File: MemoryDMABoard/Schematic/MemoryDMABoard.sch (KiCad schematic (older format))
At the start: 32 parts, among them U19 MCM6665, U20 MCM6665, U21 MCM6665, U22 MCM6665, U23 MCM6665, U24 MCM6665, U25 MCM6665, U26 MCM6665, U27 MCM6665, U28 MCM6665, U29 MCM6665, U30 MCM6665, U31 MCM6665, U32 MCM6665, U33 MCM6665, U34 MCM6665, U35 MCM6665, U36 MCM6665, U37 MCM6665, U38 MCM6665, U39 MCM6665, U40 MCM6665, U41 MCM6665, U42 MCM6665, U43 MCM6665, U44 MCM6665, U45 MCM6665, U46 MCM6665, U47 MCM6665, U48 MCM6665, U49 MCM6665, U50 MCM6665

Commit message: Add ISA bus and labels to MemoryDMABoard.
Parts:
- added C19, C20, C21, C22, C23, C24, C25, C26, C27, C28, C29, C30, C31, C32, C33, C34, C35, C36, C37, C38, C39, C40, C41, C42, C43, C44, C45, C46, C47, C48, C49, C50, C51, C52, C53, C54, C55, C56: 0.1uF, symbol Device:C
- added J0: Bus_ISA_8bit, symbol 00Custom:Bus_ISA_8bit
- added R10, R8: 56R, symbol Device:R
- added R5, R6, R7, R9: 33R, symbol Device:R
- added RP1: 56R, symbol Device:R_Pack08
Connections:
- net +5V: now also C19.1, C20.1, C21.1, C22.1, C23.1, C24.1, C25.1, C26.1, C27.1, C28.1, C29.1, C30.1, C31.1, C32.1, C33.1, C34.1, C35.1, C36.1, C37.1, C38.1, C39.1, C40.1, C41.1, C42.1, C43.1, C44.1, C45.1, C46.1, C47.1, C48.1, C49.1, C50.1, C51.1, C52.1, C53.1, C54.1, C55.1, C56.1, J0.3 (VCC)
- net DMA00: now also RP1.3 (R3.1)
- net DMA01: now also RP1.6 (R6.1)
- net DMA02: now also RP1.2 (R2.1)
- net DMA03: now also RP1.1 (R1.1)
- net DMA04: now also RP1.8 (R8.1)
- net DMA05: now also RP1.5 (R5.1)
- net DMA06: now also RP1.4 (R4.1)
- net DMA07: now also RP1.7 (R7.1)
- net GND: now also C19.2, C20.2, C21.2, C22.2, C23.2, C24.2, C25.2, C26.2, C27.2, C28.2, C29.2, C30.2, C31.2, C32.2, C33.2, C34.2, C35.2, C36.2, C37.2, C38.2, C39.2, C40.2, C41.2, C42.2, C43.2, C44.2, C45.2, C46.2, C47.2, C48.2, C49.2, C50.2, C51.2, C52.2, C53.2, C54.2, C55.2, C56.2, J0.1 (GND), J0.10 (GND), J0.31 (GND)
- net _~CAS: now also R8.1
- net _~RAS0: now also R5.1
- net _~RAS1: now also R6.1
- net _~RAS2: now also R7.1
- net _~RAS3: now also R9.1
- net _~WR: now also R10.1
- new net AEN: J0.42 (AEN)
- new net BUSA00: J0.62 (BA00)
- new net BUSA01: J0.61 (BA01)
- new net BUSA02: J0.60 (BA02)
- new net BUSA03: J0.59 (BA03)
- new net BUSA04: J0.58 (BA04)
- new net BUSA05: J0.57 (BA05)
- new net BUSA06: J0.56 (BA06)
- new net BUSA07: J0.55 (BA07)
- new net BUSA08: J0.54 (BA08)
- new net BUSA09: J0.53 (BA09)
- new net BUSA10: J0.52 (BA10)
- new net BUSA11: J0.51 (BA11)
- new net BUSA12: J0.50 (BA12)
- new net BUSA13: J0.49 (BA13)
- new net BUSA14: J0.48 (BA14)
- new net BUSA15: J0.47 (BA15)
- new net BUSA16: J0.46 (BA16)
- new net BUSA17: J0.45 (BA17)
- new net BUSA18: J0.44 (BA18)
- new net BUSA19: J0.43 (BA19)
- new net BUSD00: J0.40 (DB0)
- new net BUSD01: J0.39 (DB1)
- new net BUSD02: J0.38 (DB2)
- new net BUSD03: J0.37 (DB3)
- new net BUSD04: J0.36 (DB4)
- new net BUSD05: J0.35 (DB5)
- new net BUSD06: J0.34 (DB6)
- new net BUSD07: J0.33 (DB7)
- new net CLK: J0.20 (CLK)
- new net DMATC: J0.27 (TC)
- new net MA00: RP1.14 (R3.2)
- new net MA01: RP1.11 (R6.2)
- new net MA02: RP1.15 (R2.2)
- new net MA03: RP1.16 (R1.2)
- new net MA04: RP1.9 (R8.2)
- new net MA05: RP1.12 (R5.2)
- new net MA06: RP1.13 (R4.2)
- new net MA07: RP1.10 (R7.2)
- new net OSC: J0.30 (OSC)
- new net READY: J0.41 (IO_READY)
- new net RESET: J0.2 (RESET)
- new net ~BREQ: J0.22 (IRQ6)
- new net ~CAS: R8.2
- new net ~DACK1: J0.17 (~DACK1)
- new net ~DACK3: J0.15 (~DACK3)
- new net ~DRQ1: J0.18 (DRQ1)
- new net ~DRQ3: J0.16 (DRQ3)
- new net ~FDCDMACK: J0.26 (~DACK2)
- new net ~FDCDMARQ: J0.6 (DRQ2)
- new net ~IOR: J0.14 (~IOR)
- new net ~IOW: J0.13 (~IOW)
- new net ~MEMR: J0.12 (~SMEMR)
- new net ~MEMW: J0.11 (~SMEMW)
- new net ~RAS0: R5.2
- new net ~RAS1: R6.2
- new net ~RAS2: R7.2
- new net ~RAS3: R9.2
- new net ~REFRESH: J0.19 (~DACK0)
- new net ~RFSHRQ: J0.21 (IRQ7)
- new net ~WR: R10.2
- no-connect marks 32 -> 42
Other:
- note added: "DRAM SECTION (Tandy Schematic Sheet 2)"
- note added: "NOTE: Bus pin numbers are flipped \nfrom the Tandy Schematic. Tandy \nnumbers are 1-31 down the right \nside and 32-62 down the left side."
- moved on the sheet: U19, U20, U21, U22, U23, U24, U25, U26, U27, U28, U29, U30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

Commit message: Add ISA BUS buffering to MemoryDMABoard schematic.
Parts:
- added C1, C10, C11, C12, C13, C14, C15, C16, C17, C18, C2, C3, C4, C5, C6, C7, C8, C9: 0.1uF, symbol Device:C
- added R3: 2K2, symbol Device:R
- added U1, U11, U7: 74LS244, symbol 74xx:74LS244
- added U15, U17: 74LS245, symbol 74xx:74LS245
- added U2: 74LS04, symbol 74xx:74LS04
- added U?: 8237, Package_DIP:DIP-40_W15.24mm, symbol Interface:8237
- C51, C52, C53, C54, C55, C56: value 0.1uF -> 68uF; symbol Device:C -> Device:CP
- renumbered J0 to J1
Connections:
- net +5V: now also C1.1, C10.1, C11.1, C12.1, C13.1, C14.1, C15.1, C16.1, C17.1, C18.1, C2.1, C3.1, C4.1, C5.1, C6.1, C7.1, C8.1, C9.1, R3.1, U1.20 (VCC), U11.20 (VCC), U15.20 (VCC), U17.20 (VCC), U7.20 (VCC)
- net AEN: now also U1.4 (I1a)
- net BUSA00: now also U15.14 (B4)
- net BUSA01: now also U15.13 (B5)
- net BUSA02: now also U15.12 (B6)
- net BUSA03: now also U15.11 (B7)
- net BUSA04: now also U11.2 (I0a)
- net BUSA05: now also U11.15 (I2b)
- net BUSA06: now also U11.13 (I1b)
- net BUSA07: now also U11.4 (I1a)
- net BUSA08: now also U7.11 (I0b)
- net BUSA09: now also U7.13 (I1b)
- net BUSA10: now also U7.15 (I2b)
- net BUSA11: now also U7.17 (I3b)
- net BUSA12: now also U7.8 (I3a)
- net BUSA13: now also U7.6 (I2a)
- net BUSA14: now also U7.4 (I1a)
- net BUSA15: now also U7.2 (I0a)
- net BUSA16: now also U1.8 (I3a)
- net BUSA17: now also U1.11 (I0b)
- net BUSA18: now also U1.13 (I1b)
- net BUSA19: now also U1.17 (I3b)
- net BUSD00: now also U17.18 (B0)
- net BUSD01: now also U17.17 (B1)
- net BUSD02: now also U17.16 (B2)
- net BUSD03: now also U17.15 (B3)
- net BUSD04: now also U17.14 (B4)
- net BUSD05: now also U17.13 (B5)
- net BUSD06: now also U17.12 (B6)
- net BUSD07: now also U17.11 (B7)
- net CLK: now also U1.15 (I2b)
- net D00: now also U17.2 (A0)
- net D01: now also U17.3 (A1)
- net D02: now also U17.4 (A2)
- net D03: now also U17.5 (A3)
- net D04: now also U17.6 (A4)
- net D05: now also U17.7 (A5)
- net D06: now also U17.8 (A6)
- net D07: now also U17.9 (A7)
- net DMATC: now also U11.9 (O0b)
- net GND: now also C1.2, C10.2, C11.2, C12.2, C13.2, C14.2, C15.2, C16.2, C17.2, C18.2, C2.2, C3.2, C4.2, C5.2, C6.2, C7.2, C8.2, C9.2, U1.1 (OEa), U1.10 (GND), U1.19 (OEb), U11.1 (OEa), U11.10 (GND), U11.19 (OEb), U15.10 (GND), U15.19 (CE), U17.10 (GND), U7.1 (OEa), U7.10 (GND), U7.19 (OEb)
- net OSC: now also U11.8 (I3a)
- net READY: now also U1.6 (I2a)
- net RESET: now also U1.2 (I0a)
- net ~BREQ: now also U11.3 (O3b)
- net ~IOR: now also U15.15 (B3)
- net ~IOW: now also U15.16 (B2)
- net ~MEMR: now also U15.17 (B1)
- net ~MEMW: now also U15.18 (B0)
- new net A00: U15.6 (A4)
- new net A01: U15.7 (A5)
- new net A02: U15.8 (A6)
- new net A03: U15.9 (A7)
- new net A04: U11.18 (O0a)
- new net A05: U11.5 (O2b)
- new net A06: U11.7 (O1b)
- new net A07: U11.16 (O1a)
- new net A08: U7.9 (O0b)
- new net A09: U7.7 (O1b)
- new net A10: U7.5 (O2b)
- new net A11: U7.3 (O3b)
- new net A12: U7.12 (O3a)
- new net A13: U7.14 (O2a)
- new net A14: U7.16 (O1a)
- new net A15: U7.18 (O0a)
- new net A16: U1.12 (O3a)
- new net A17: U1.9 (O0b)
- new net A18: U1.7 (O1b)
- new net A19: U1.3 (O3b)
- new net BRDY: U1.14 (O2a)
- new net DBDIR: U17.1 (A->B)
- new net DMAAEN: U15.1 (A->B)
- new net DMACLK: U2.6, U?.12 (CLK)
- new net HSCLK: U11.12 (O3a)
- new net _8237_HLDA: U1.16 (O1a), U?.7 (HLDA)
- new net _8237_HRQ: U2.1, U?.10 (HRQ)
- new net _8237_RESET: U1.18 (O0a), U?.13 (RESET)
- new net _8237_~EOP: R3.2, U2.3, U?.36 (~EOP~)
- new net _CLK_BUF: U1.5 (O2b), U2.5
- new net _DMATC_UNBUF: U11.11 (I0b), U2.4
- new net _~BREQ~_UNBUF: U11.17 (I3b), U2.2
- new net ~DBEN: U17.19 (CE)
- new net ~IR: U15.5 (A3)
- new net ~IW: U15.4 (A2)
- new net ~MR: U15.3 (A1)
- new net ~MW: U15.2 (A0)
- no-connect marks 42 -> 44
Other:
- note added: "BUS Buffering"
- note added: "ISA BUS"
- moved on the sheet: C19, C20, C21, C22, C23, C24, C25, C26, C27, C28, C29, C30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

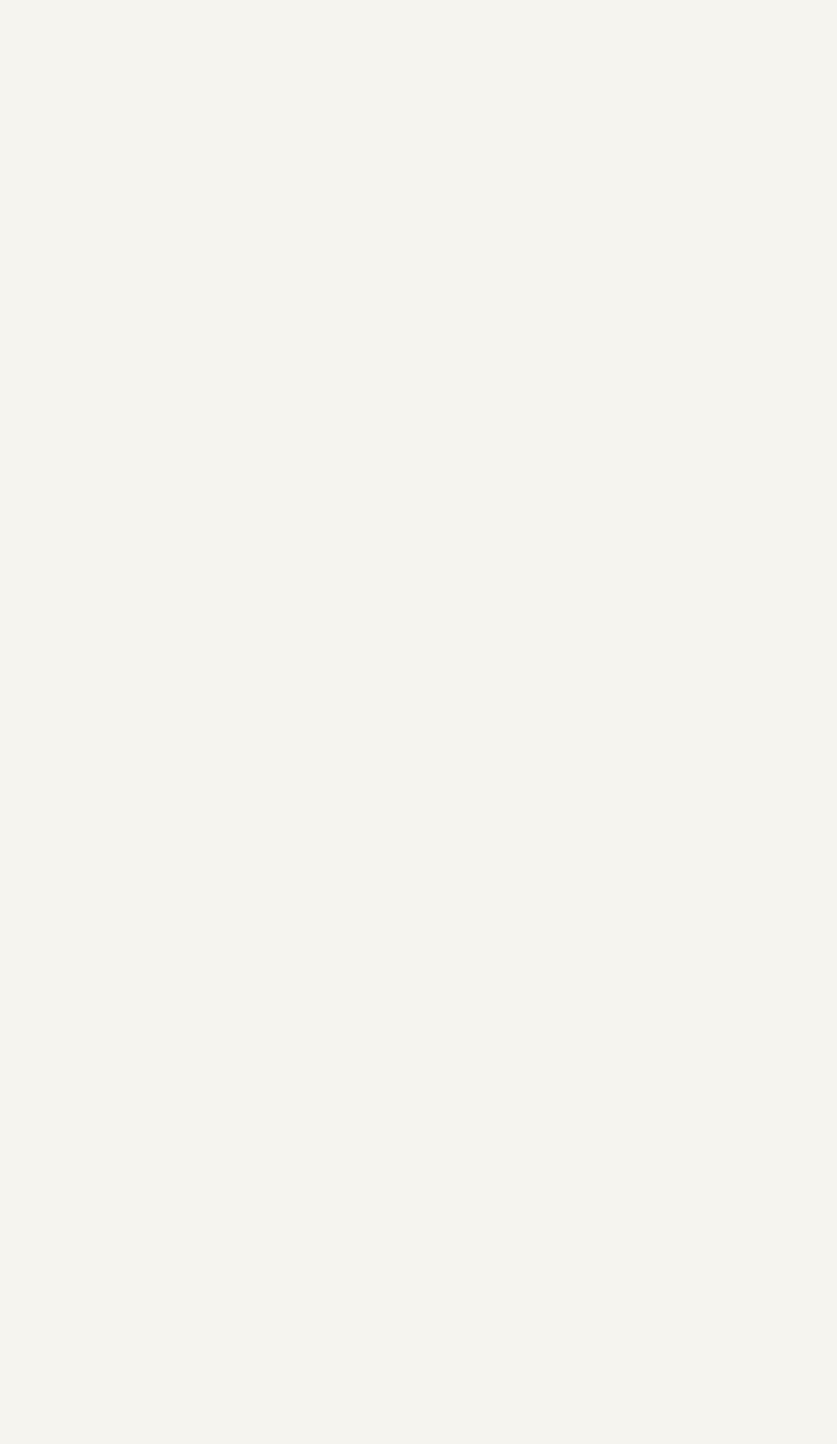
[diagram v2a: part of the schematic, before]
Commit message: Add DRAM address multiplexing.
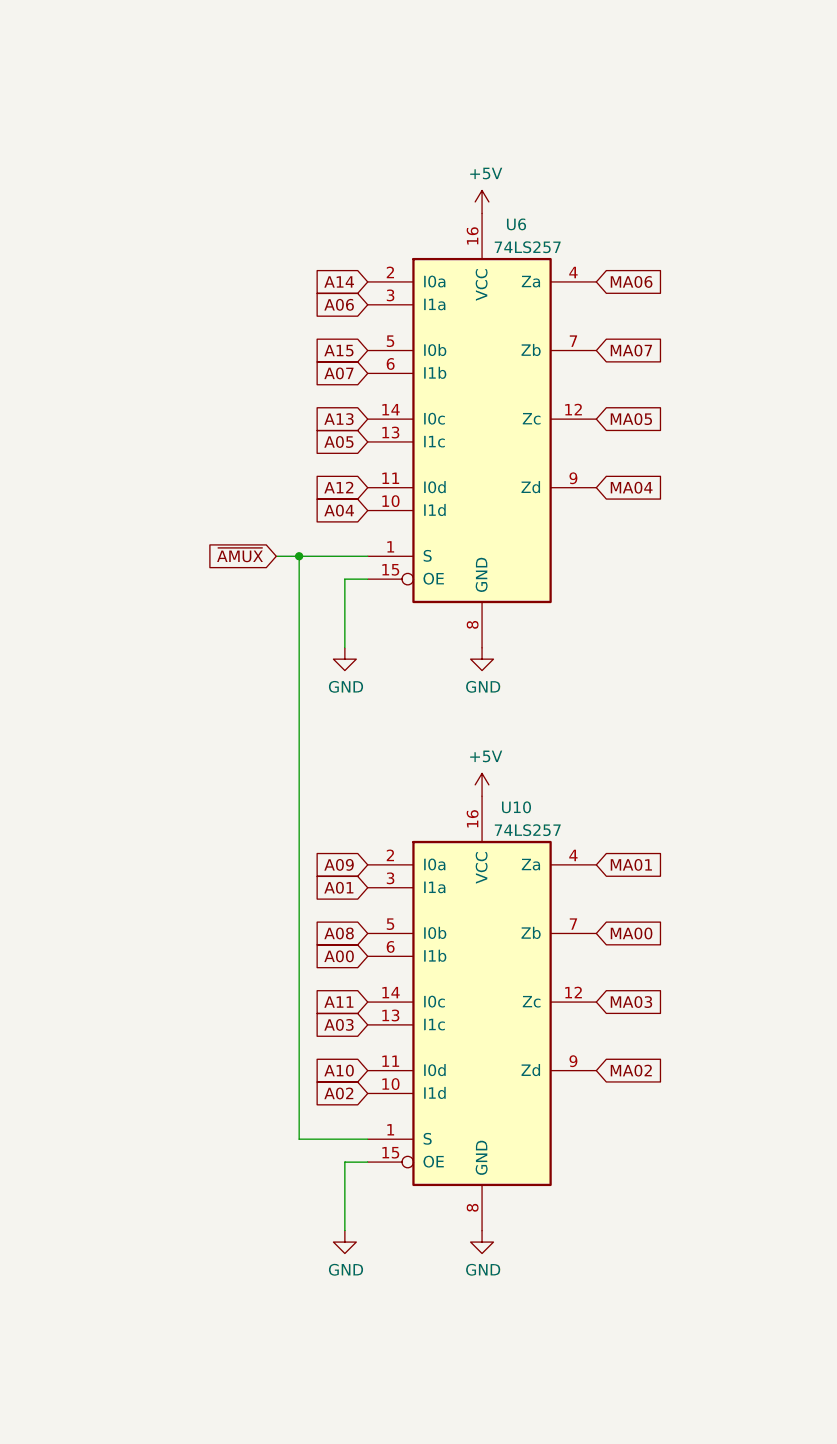
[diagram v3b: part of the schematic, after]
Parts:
- added U10, U6: 74LS257, symbol 74xx:74LS257
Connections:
- net +5V: now also U10.16 (VCC), U6.16 (VCC)
- net A00: now also U10.6 (I1b)
- net A01: now also U10.3 (I1a)
- net A02: now also U10.10 (I1d)
- net A03: now also U10.13 (I1c)
- net A04: now also U6.10 (I1d)
- net A05: now also U6.13 (I1c)
- net A06: now also U6.3 (I1a)
- net A07: now also U6.6 (I1b)
- net A08: now also U10.5 (I0b)
- net A09: now also U10.2 (I0a)
- net A10: now also U10.11 (I0d)
- net A11: now also U10.14 (I0c)
- net A12: now also U6.11 (I0d)
- net A13: now also U6.14 (I0c)
- net A14: now also U6.2 (I0a)
- net A15: now also U6.5 (I0b)
- net GND: now also U10.15 (OE), U10.8 (GND), U6.15 (OE), U6.8 (GND)
- net MA00: now also U10.7 (Zb)
- net MA01: now also U10.4 (Za)
- net MA02: now also U10.9 (Zd)
- net MA03: now also U10.12 (Zc)
- net MA04: now also U6.9 (Zd)
- net MA05: now also U6.12 (Zc)
- net MA06: now also U6.4 (Za)
- net MA07: now also U6.7 (Zb)
- new net ~AMUX: U10.1 (S), U6.1 (S)
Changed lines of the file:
@@
 Text Notes 1250 1000 0    118  ~ 0
 ISA BUS
+$Comp
+L 74xx:74LS257 U6
+U 1 1 606B6E2F
+P 27100 25200
+F 0 "U6" H 27250 26050 50  0000 C CNN
+F 1 "74LS257" H 27300 25950 50  0000 C CNN
+F 2 "" H 27100 25200 50  0001 C CNN
+F 3 "http://www.ti.com/lit/gpn/sn74LS257" H 27100 25200 50  0001 C CNN
+	1    27100 25200
+	1    0    0    -1
+$EndComp
+$Comp
+L power:GND #PWR?
+U 1 1 606B9008
+P 27100 26200
+F 0 "#PWR?" H 27100 25950 50  0001 C CNN
+F 1 "GND" H 27105 26027 50  0000 C CNN
+F 2 "" H 27100 26200 50  0001 C CNN
+F 3 "" H 27100 26200 50  0001 C CNN
+	1    27100 26200
+	1    0    0    -1
+$EndComp
+$Comp
+L power:+5V #PWR?
+U 1 1 606B972A
+P 27100 24300
+F 0 "#PWR?" H 27100 24150 50  0001 C CNN
+F 1 "+5V" H 27115 24473 50  0000 C CNN
+F 2 "" H 27100 24300 50  0001 C CNN
+F 3 "" H 27100 24300 50  0001 C CNN
+	1    27100 24300
+	1    0    0    -1
+$EndComp
+$Comp
+L power:GND #PWR?
+U 1 1 606BA42C
+P 26500 26200
+F 0 "#PWR?" H 26500 25950 50  0001 C CNN
+F 1 "GND" H 26505 26027 50  0000 C CNN
+F 2 "" H 26500 26200 50  0001 C CNN
+F 3 "" H 26500 26200 50  0001 C CNN
+	1    26500 26200
+	1    0    0    -1
+$EndComp
+Wire Wire Line
+	26600 25900 26500 25900
+Wire Wire Line
+	26500 25900 26500 26200
+$Comp
+L 74xx:74LS257 U10
+U 1 1 606D1323
+P 27100 27750
+F 0 "U10" H 27250 28600 50  0000 C CNN
+F 1 "74LS257" H 27300 28500 50  0000 C CNN
+F 2 "" H 27100 27750 50  0001 C CNN
+F 3 "http://www.ti.com/lit/gpn/sn74LS257" H 27100 27750 50  0001 C CNN
+	1    27100 27750
+	1    0    0    -1
+$EndComp
+$Comp
+L power:GND #PWR?
+U 1 1 606D2B39
+P 27100 28750
+F 0 "#PWR?" H 27100 28500 50  0001 C CNN
+F 1 "GND" H 27105 28577 50  0000 C CNN
+F 2 "" H 27100 28750 50  0001 C CNN
+F 3 "" H 27100 28750 50  0001 C CNN
+	1    27100 28750
+	1    0    0    -1
+$EndComp
+$Comp
+L power:+5V #PWR?
+U 1 1 606D2B43
+P 27100 26850
+F 0 "#PWR?" H 27100 26700 50  0001 C CNN
+F 1 "+5V" H 27115 27023 50  0000 C CNN
+F 2 "" H 27100 26850 50  0001 C CNN
+F 3 "" H 27100 26850 50  0001 C CNN
+	1    27100 26850
+	1    0    0    -1
+$EndComp
+$Comp
+L power:GND #PWR?
+U 1 1 606D2B4D
+P 26500 28750
+F 0 "#PWR?" H 26500 28500 50  0001 C CNN
+F 1 "GND" H 26505 28577 50  0000 C CNN
+F 2 "" H 26500 28750 50  0001 C CNN
+F 3 "" H 26500 28750 50  0001 C CNN
+	1    26500 28750
+	1    0    0    -1
+$EndComp
+Wire Wire Line
+	26600 28450 26500 28450
+Wire Wire Line
+	26500 28450 26500 28750
+Text GLabel 26600 24600 0    50   Input ~ 0
+A14
+Text GLabel 26600 24700 0    50   Input ~ 0
+A06
+Text GLabel 26600 24900 0    50   Input ~ 0
+A15
+Text GLabel 26600 25000 0    50   Input ~ 0
+A07
+Text GLabel 26600 25200 0    50   Input ~ 0
+A13
+Text GLabel 26600 25300 0    50   Input ~ 0
+A05
+Text GLabel 26600 25500 0    50   Input ~ 0
+A12
+Text GLabel 26600 25600 0    50   Input ~ 0
+A04
+Text GLabel 27600 24600 2    50   Input ~ 0
+MA06
+Text GLabel 27600 24900 2    50   Input ~ 0
+MA07
+Text GLabel 27600 25200 2    50   Input ~ 0
+MA05
+Text GLabel 27600 25500 2    50   Input ~ 0
+MA04
+Text GLabel 26600 27150 0    50   Input ~ 0
+A09
+Text GLabel 26600 27250 0    50   Input ~ 0
+A01
+Text GLabel 26600 27450 0    50   Input ~ 0
+A08
+Text GLabel 26600 27550 0    50   Input ~ 0
+A00
+Text GLabel 26600 27750 0    50   Input ~ 0
+A11
+Text GLabel 26600 27850 0    50   Input ~ 0
+A03
+Text GLabel 26600 28050 0    50   Input ~ 0
+A10
+Text GLabel 26600 28150 0    50   Input ~ 0
+A02
+Text GLabel 27600 27150 2    50   Input ~ 0
+MA01
+Text GLabel 27600 27450 2    50   Input ~ 0
+MA00
+Text GLabel 27600 27750 2    50   Input ~ 0
+MA03
+Text GLabel 27600 28050 2    50   Input ~ 0
+MA02
+Wire Wire Line
+	26600 28350 26300 28350
+Wire Wire Line
+	26300 28350 26300 25800
+Wire Wire Line
+	26300 25800 26600 25800
+Wire Wire Line
+	26200 25800 26300 25800
+Connection ~ 26300 25800
+Text GLabel 26200 25800 0    50   Input ~ 0
+~AMUX
 $EndSCHEMATC

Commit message: Add address driving to MemoryDMABoard schematic.
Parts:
- added R11: 470R, symbol Device:R
- added U14: 74LS373, symbol 74xx:74LS373
- added U16: 74LS125, symbol 74xx:74LS125
- added U18: 74LS670, symbol 74xx:74LS670
- added unit 6 of U2
- gave numbers to parts that had none: 1
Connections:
- net +5V: now also U13.31 (Vcc), U13.5 (PIN5), U14.20 (VCC), U16.14 (VCC), U18.16 (VCC)
- net A00: now also U18.13 (Wb)
- net A01: now also U18.14 (Wa)
- net BUSA04: now also U16.3
- net BUSA05: now also U16.6
- net BUSA06: now also U16.8
- net BUSA07: now also U16.11
- net BUSA08: now also U14.19 (O7)
- net BUSA09: now also U14.16 (O6)
- net BUSA10: now also U14.15 (O5)
- net BUSA11: now also U14.12 (O4)
- net BUSA12: now also U14.2 (O0)
- net BUSA13: now also U14.5 (O1)
- net BUSA14: now also U14.9 (O3)
- net BUSA15: now also U14.6 (O2)
- net BUSA16: now also U18.10 (Q1)
- net BUSA17: now also U18.9 (Q2)
- net BUSA18: now also U18.7 (Q3)
- net BUSA19: now also U18.6 (Q4)
- net D00: now also U13.30 (DB0), U14.18 (D7), U18.15 (D1)
- net D01: now also U13.29 (DB1), U14.17 (D6), U18.1 (D2)
- net D02: now also U13.28 (DB2), U14.14 (D5), U18.2 (D3)
- net D03: now also U13.27 (DB3), U14.13 (D4), U18.3 (D4)
- net D04: now also U13.26 (DB4), U14.3 (D0)
- net D05: now also U13.23 (DB5), U14.4 (D1)
- net D06: now also U13.22 (DB6), U14.8 (D3)
- net D07: now also U13.21 (DB7), U14.7 (D2)
- net DMAAEN: now also U13.9 (AEN), R11.1, U2.13
- net GND: now also U13.20 (Vss), R11.2, U14.10 (GND), U16.7 (GND), U18.8 (GND)
- net ~DACK3: now also U18.5 (Ra)
- net ~FDCDMACK: now also U18.4 (Rb)
- net ~IR: now also U13.1 (~IOR~)
- net ~IW: now also U13.2 (~IOW~)
- net ~MR: now also U13.3 (~MEMR~)
- net ~MW: now also U13.4 (~MEMW~)
- net DMAA04: now reaches U13.37 (A4)
- net DMAA04: now also U16.2
- net DMAA05: now reaches U13.38 (A5)
- net DMAA05: now also U16.5
- net DMAA06: now reaches U13.39 (A6)
- net DMAA06: now also U16.9
- net DMAA07: now reaches U13.40 (A7)
- net DMAA07: now also U16.12
- net ADSTB: now reaches U13.8 (ADSTB)
- net ADSTB: now also U14.11 (LE)
- new net ~DMAAEN: U14.1 (OE), U16.1, U16.10, U16.13, U16.4, U18.11 (~Er), U2.12
- new net ~WPRCS: U18.12 (~Ew)
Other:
- moved on the sheet: U13

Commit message: Add partial glue logic to MemoryDMABoard schematic.
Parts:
- added E1, E2, E3, E4: Pin, symbol Connector_Generic:Conn_01x01
- added R1, R2: 2K2, symbol Device:R
- added unit 7 of U2
- added U5, U9: 82S153, symbol 00Custom:82S153
- added U8: 74LS260, symbol 00Custom:74LS260
- added U?: 74LS32, symbol 74xx:74LS32
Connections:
- net +5V: now also R1.1, R2.1, U2.14 (VCC), U5.20 (Vcc), U8.14 (Vcc), U9.20 (Vcc)
- net A00: now also U13.32 (A0)
- net A01: now also U13.33 (A1)
- net A02: now also U13.34 (A2), U9.8 (I7)
- net A03: now also U13.35 (A3), U9.7 (I6)
- net A04: now also U9.6 (I5)
- net A05: now also U9.5 (I4)
- net A06: now also U9.4 (I3)
- net A07: now also U9.3 (I2)
- net A08: now also U8.12 (AI4)
- net A09: now also U8.13 (AI3)
- net A10: now also U8.1 (AI0)
- net A11: now also U8.2 (AI1)
- net A12: now also U8.11 (BI1)
- net A13: now also U8.10 (BI2)
- net A14: now also U8.8 (BI4), U8.9 (BI3)
- net A16: now also U5.7 (I6)
- net A17: now also U5.6 (I5)
- net A18: now also U5.5 (I4)
- net A19: now also U5.4 (I3)
- net DBDIR: now also U9.17 (B7)
- net DMAAEN: now also U9.13 (B3)
- net GND: now also E2.1 (Pin_1), E4.1 (Pin_1), U2.7 (GND), U5.10 (GND), U8.3 (AI2), U8.4 (BI0), U8.7 (GND), U9.10 (GND)
- net ~CAS: now also U5.12 (B2)
- net ~DACK1: now also U13.24 (DACK1)
- net ~DACK3: now also U13.15 (DACK3)
- net ~DBEN: now also U9.16 (B6)
- net ~DRQ1: now also U13.18 (DREQ1)
- net ~DRQ3: now also U13.16 (DREQ3)
- net ~FDCDMACK: now also U13.14 (DACK2)
- net ~FDCDMARQ: now also U13.17 (DREQ2)
- net ~IR: now also U9.9 (B0)
- net ~IW: now also U9.11 (B1)
- net ~MR: now also U5.1 (I0), U9.12 (B2)
- net ~MW: now also U5.2 (I1), U?.4
- net ~RAS0: now also U5.15 (B5)
- net ~RAS1: now also U5.16 (B6)
- net ~RAS2: now also U5.17 (B7)
- net ~RAS3: now also U5.18 (B8)
- net ~REFRESH: now also U13.25 (DACK0), U5.3 (I2)
- net ~RFSHRQ: now also U13.19 (DREQ0)
- net ~WPRCS: now also U9.14 (B4)
- net ~WR: now also U?.6
- net ~DMACS: now reaches U13.11 (~CS~)
- net ~DMACS: now also U9.15 (B5)
- net SRDY: now reaches U13.6 (READY)
- new net: U5.19 (B9), U?.5
- new net FIRSTBD: E3.1 (Pin_1), R2.2, U5.14 (B4), U9.19 (B9)
- new net MEMADD: U5.13 (B3), U9.18 (B8)
- new net _LOW_ADDR_RANGE_A: U8.5 (AO), U9.1 (I0)
- new net _LOW_ADDR_RANGE_B: U8.6 (BO), U9.2 (I1)
- new net _RAM_SIZE: E1.1 (Pin_1), R1.2, U5.11 (B1)
